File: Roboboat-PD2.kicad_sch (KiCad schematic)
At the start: 29 parts, among them J1 12V, J10 Motor, J11 Motor, J12 Motor, J13 Motor, J14 5V, J15 14.4V, J16 PGOOD, J2 Bucky, J3 Jetson, J4 Motor, J5 Motor, J6 Motor, J7 Motor, J8 Motor, J9 Motor, SW1 Jumper, U1 AOZ2367QI-11

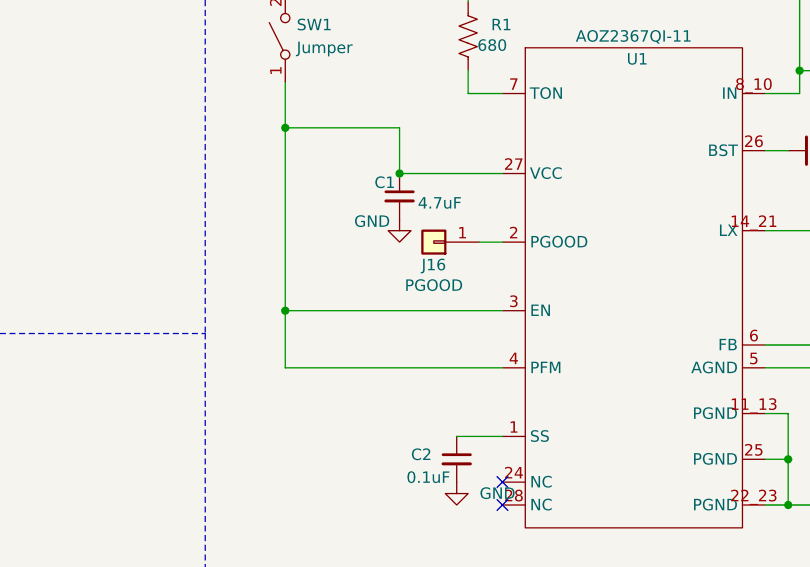
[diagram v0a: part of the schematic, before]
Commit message: add 0.1uF capacitor to PGOOD
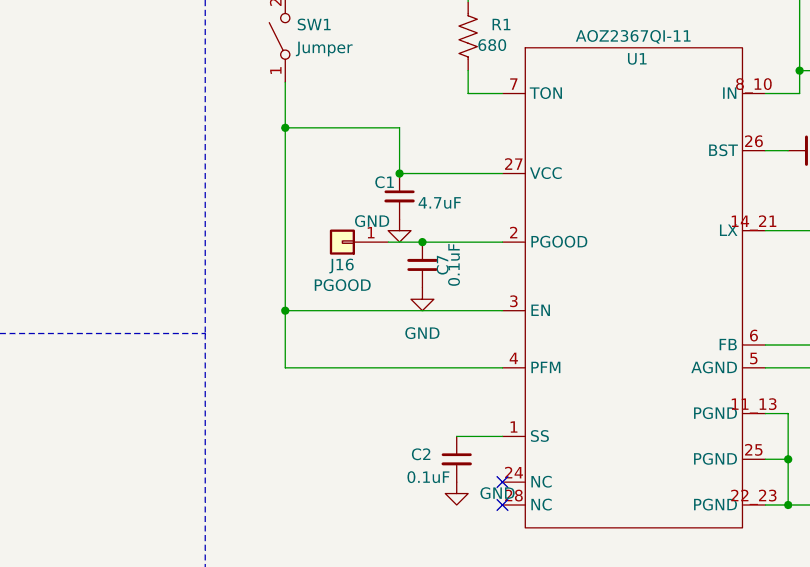
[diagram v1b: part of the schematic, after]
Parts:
- added C7: 0.1uF, Capacitor_SMD:C_1206_3216Metric, symbol Device:C_Small
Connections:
- net GND: now also C7.1
- net at J16.1 (Pin_1), U1.2 (PGOOD): now also C7.2
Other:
- moved on the sheet: J16
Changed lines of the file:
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@@
 	)
 	(junction
+		(at 118.11 66.04)
+		(diameter 0)
+		(color 0 0 0 0)
+	)
+	(junction
 		(at 49.53 110.49)
 		(diameter 0)
@@
 	(wire
 		(pts
-			(xy 124.46 66.04) (xy 127 66.04)
+			(xy 114.3 66.04) (xy 118.11 66.04)
 		)
 		(stroke
@@
 	(wire
 		(pts
+			(xy 118.11 66.04) (xy 127 66.04)
+		)
+		(stroke
+			(width 0)
+			(type default)
+		)
+	)
+	(wire
+		(pts
 			(xy 172.72 64.77) (xy 173.99 64.77)
 		)
@@
 	(symbol
 		(lib_id "power:GND")
+		(at 118.11 71.12 0)
+		(unit 1)
+		(exclude_from_sim no)
+		(in_bom yes)
+		(on_board yes)
+		(dnp no)
+		(fields_autoplaced yes)
+		(property "Reference" "#PWR019"
+			(at 118.11 77.47 0)
+			(effects
+				(font
+					(size 1.27 1.27)
+				)
+				(hide yes)
+			)
+		)
+		(property "Value" "GND"
+			(at 118.11 76.2 0)
+			(effects
+				(font
+					(size 1.27 1.27)
+				)
+			)
+		)
+		(property "Footprint" ""
+			(at 118.11 71.12 0)
+			(effects
+				(font
+					(size 1.27 1.27)
+				)
+				(hide yes)
+			)
+		)
+		(property "Datasheet" ""
+			(at 118.11 71.12 0)
+			(effects
+				(font
+					(size 1.27 1.27)
+				)
+				(hide yes)
+			)
+		)
+		(property "Description" "Power symbol creates a global label with name \"GND\" , ground"
+			(at 118.11 71.12 0)
+			(effects
+				(font
+					(size 1.27 1.27)
+				)
+				(hide yes)
+			)
+		)
+		(pin "1"
+		)
+		(instances
+			(project ""
+				(path "/9a1496f4-7cef-4d33-8239-9c2f43ceb177"
+					(reference "#PWR019")
+					(unit 1)
+				)
+			)
+		)
+	)
+	(symbol
+		(lib_id "power:GND")
 		(at 54.61 55.88 0)
 		(unit 1)
@@
 	(symbol
 		(lib_id "Device:C_Small")
+		(at 118.11 68.58 180)
+		(unit 1)
+		(exclude_from_sim no)
+		(in_bom yes)
+		(on_board yes)
+		(dnp no)
+		(property "Reference" "C7"
+			(at 120.396 68.58 90)
+			(effects
+				(font
+					(size 1.27 1.27)
+				)
+			)
+		)
+		(property "Value" "0.1uF"
+			(at 121.666 68.58 90)
+			(effects
+				(font
+					(size 1.27 1.27)
+				)
+			)
+		)
+		(property "Footprint" "Capacitor_SMD:C_1206_3216Metric"
+			(at 118.11 68.58 0)
+			(effects
+				(font
+					(size 1.27 1.27)
+				)
+				(hide yes)
+			)
+		)
+		(property "Datasheet" "~"
+			(at 118.11 68.58 0)
+			(effects
+				(font
+					(size 1.27 1.27)
+				)
+				(hide yes)
+			)
+		)
+		(property "Description" "Unpolarized capacitor, small symbol"
+			(at 118.11 68.58 0)
+			(effects
+				(font
+					(size 1.27 1.27)
+				)
+				(hide yes)
+			)
+		)
+		(pin "2"
+		)
+		(pin "1"
+		)
+		(instances
+			(project "Roboboat-PD2"
+				(path "/9a1496f4-7cef-4d33-8239-9c2f43ceb177"
+					(reference "C7")
+					(unit 1)
+				)
+			)
+		)
+	)
+	(symbol
+		(lib_id "Device:C_Small")
 		(at 180.34 49.53 0)
 		(unit 1)
@@
 	(symbol
 		(lib_id "Connector_Generic:Conn_01x01")
-		(at 119.38 66.04 180)
+		(at 109.22 66.04 180)
 		(unit 1)
 		(exclude_from_sim no)
@@
 		(dnp no)
 		(property "Reference" "J16"
-			(at 119.38 68.58 0)
+			(at 109.22 68.58 0)
 			(effects
 				(font
@@
 		)
 		(property "Value" "PGOOD"
-			(at 119.38 70.866 0)
+			(at 109.22 70.866 0)
 			(effects
 				(font
@@
 		)
 		(property "Footprint" "Connector_JST:JST_XH_B1B-XH-AM_1x01_P2.50mm_Vertical"
-			(at 119.38 66.04 0)
+			(at 109.22 66.04 0)
 			(effects
 				(font
@@
 		)
 		(property "Datasheet" "~"
-			(at 119.38 66.04 0)
+			(at 109.22 66.04 0)
 			(effects
 				(font
@@
 		)
 		(property "Description" "Generic connector, single row, 01x01, script generated (kicad-library-utils/schlib/autogen/connector/)"
-			(at 119.38 66.04 0)
+			(at 109.22 66.04 0)
 			(effects
 				(font

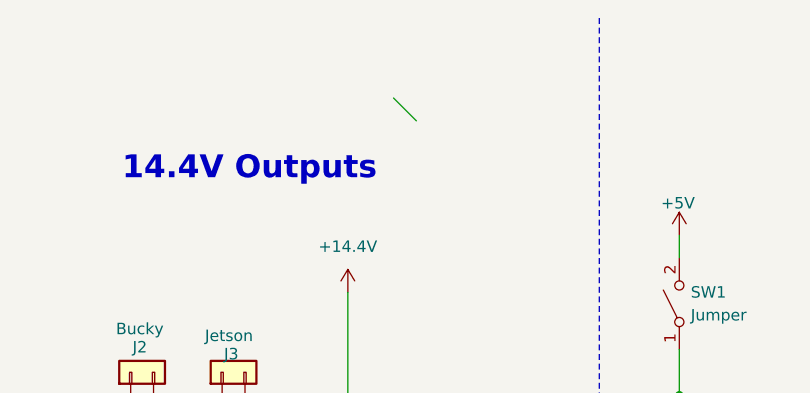
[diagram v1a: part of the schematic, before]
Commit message: move R1, R2, R3, correct fuse footprint
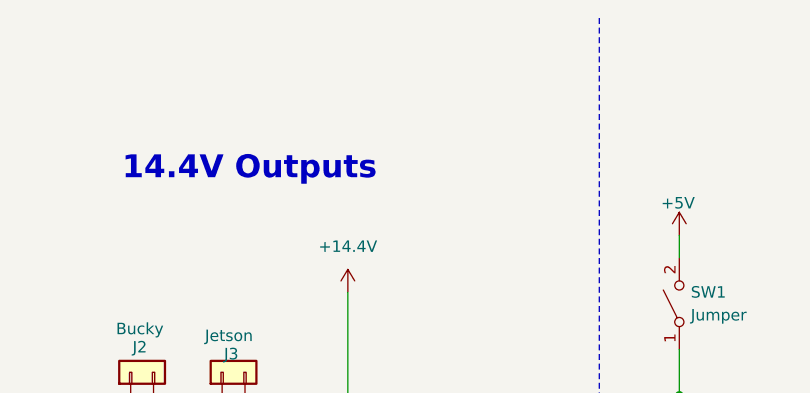
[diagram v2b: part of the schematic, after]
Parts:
- F1: footprint footprints:FUSE_0ZCF0075AF2C -> Fuse:Fuse_1812_4532Metric
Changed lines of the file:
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@@
 		(at 127 92.71)
-	)
-	(bus_entry
-		(at 71.12 20.32)
-		(size 2.54 2.54)
-		(stroke
-			(width 0)
-			(type default)
-		)
 	)
 	(wire
@@
 			)
 		)
-		(property "Footprint" "footprints:FUSE_0ZCF0075AF2C"
+		(property "Footprint" "Fuse:Fuse_1812_4532Metric"
 			(at 52.07 60.96 0)
 			(effects

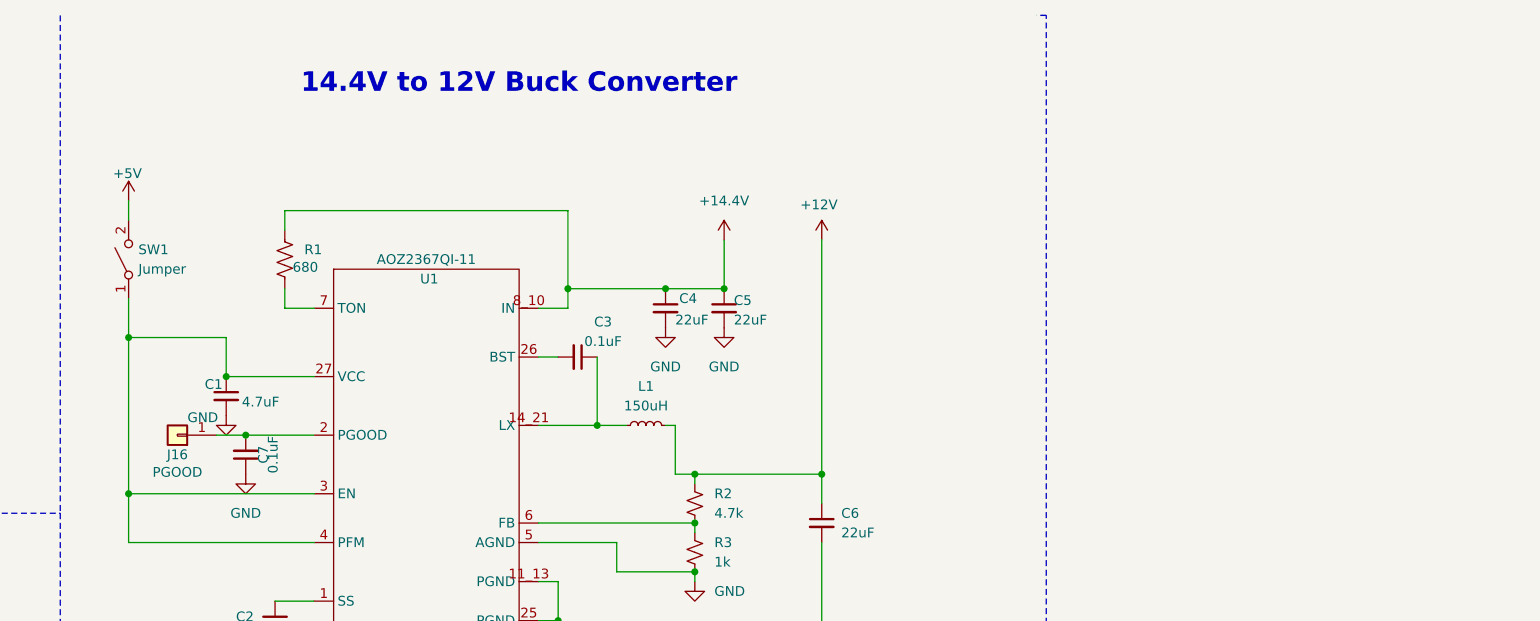
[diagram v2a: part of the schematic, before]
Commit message: add mounting holes and test points to schematic
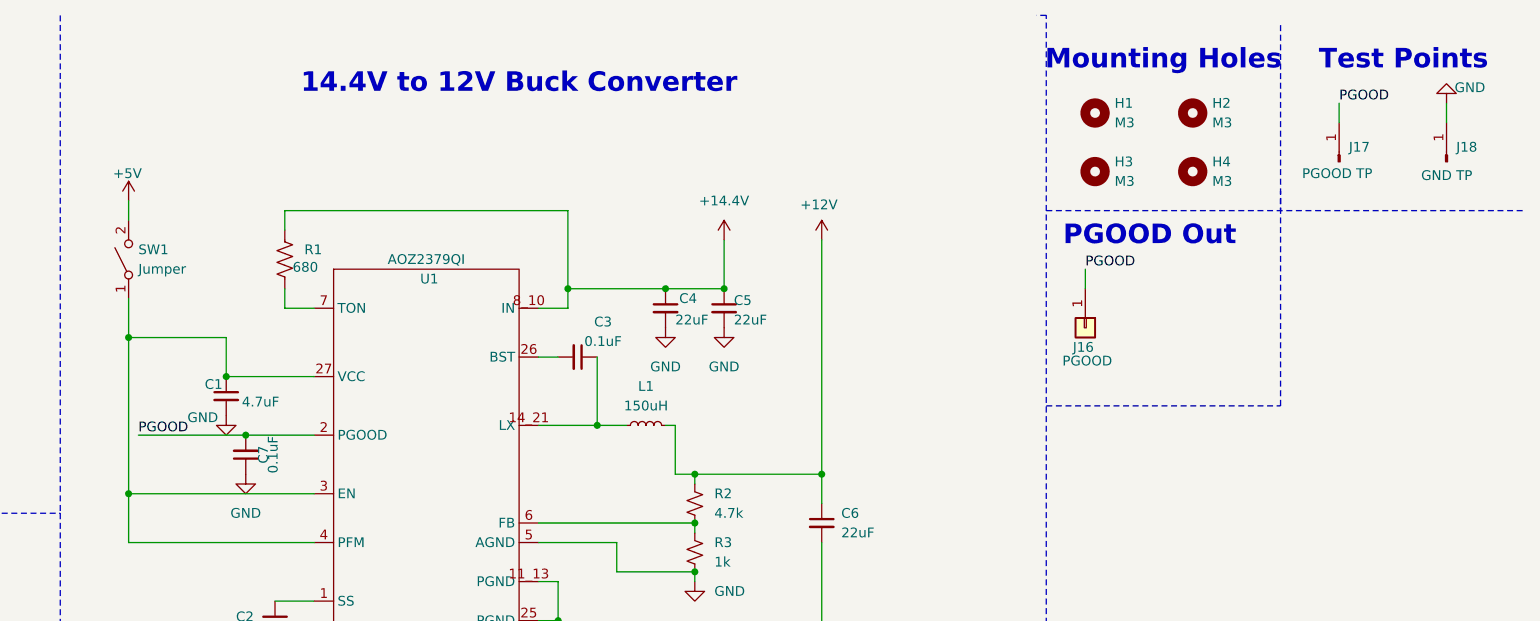
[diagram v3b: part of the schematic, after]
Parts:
- added H1, H2, H3, H4: M3, MountingHole:MountingHole_3.2mm_M3, symbol Mechanical:MountingHole
- added J17: PGOOD TP, TestPoint:TestPoint_Keystone_5010-5014_Multipurpose, symbol Connector:Conn_01x01_Pin
- added J18: GND TP, TestPoint:TestPoint_Keystone_5010-5014_Multipurpose, symbol Connector:Conn_01x01_Pin
- U1: value AOZ2367QI-11 -> AOZ2379QI
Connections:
- net GND: now also J18.1 (Pin_1)
- net PGOOD: now reaches C7.2, J16.1 (Pin_1), U1.2 (PGOOD)
- net PGOOD: now also J17.1 (Pin_1)
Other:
- note added: "Mounting Holes"
- note added: "PGOOD Out"
- note added: "Test Points"

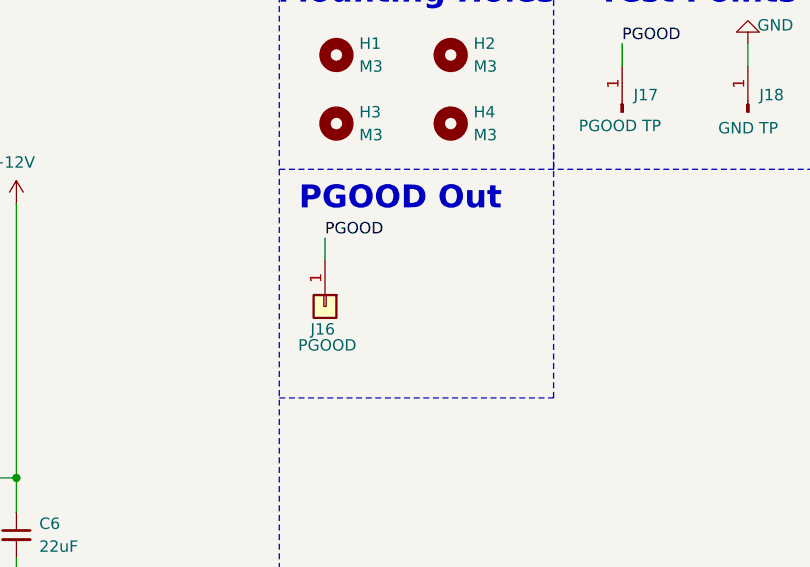
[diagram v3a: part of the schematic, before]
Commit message: add ground to PGOOD output
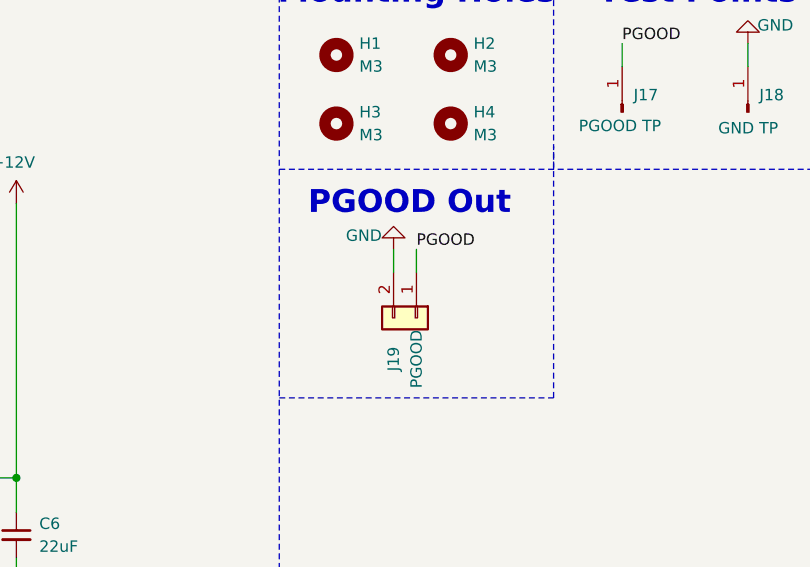
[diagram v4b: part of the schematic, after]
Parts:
- removed J16: PGOOD, Connector_JST:JST_XH_B1B-XH-AM_1x01_P2.50mm_Vertical, symbol Connector_Generic:Conn_01x01
- added J19: PGOOD, Connector_JST:JST_VH_B2P-VH-B_1x02_P3.96mm_Vertical, symbol Connector_Generic:Conn_01x02
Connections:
- net GND: now also J19.2 (Pin_2)
- net PGOOD: now also J19.1 (Pin_1)
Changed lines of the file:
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@@
-	(wire
-		(pts
-			(xy 227.33 44.45) (xy 227.33 46.99)
-		)
-		(stroke
-			(width 0)
-			(type default)
-		)
-	)
 	(wire
 		(pts
@@
 		)
 	)
+	(wire
+		(pts
+			(xy 237.49 45.72) (xy 237.49 48.26)
+		)
+		(stroke
+			(width 0)
+			(type default)
+		)
+	)
 	(polyline
 		(pts
@@
 		(pts
 			(xy 49.53 163.83) (xy 49.53 172.72)
+		)
+		(stroke
+			(width 0)
+			(type default)
+		)
+	)
+	(wire
+		(pts
+			(xy 234.95 45.72) (xy 234.95 48.26)
 		)
 		(stroke
@@
 	(text "PGOOD Out"
 		(exclude_from_sim no)
-		(at 235.712 40.132 0)
+		(at 236.728 40.64 0)
 		(effects
 			(font
@@
 	)
 	(label "PGOOD"
-		(at 227.33 44.45 0)
+		(at 237.49 45.72 0)
 		(fields_autoplaced yes)
 		(effects
@@
 	)
 	(symbol
-		(lib_id "Connector_Generic:Conn_01x01")
-		(at 227.33 52.07 270)
-		(unit 1)
-		(exclude_from_sim no)
-		(in_bom yes)
-		(on_board yes)
-		(dnp no)
-		(property "Reference" "J16"
-			(at 227.076 54.61 90)
-			(effects
-				(font
-					(size 1.27 1.27)
-				)
-			)
-		)
-		(property "Value" "PGOOD"
-			(at 227.584 56.388 90)
-			(effects
-				(font
-					(size 1.27 1.27)
-				)
-			)
-		)
-		(property "Footprint" "Connector_JST:JST_XH_B1B-XH-AM_1x01_P2.50mm_Vertical"
-			(at 227.33 52.07 0)
-			(effects
-				(font
-					(size 1.27 1.27)
-				)
-				(hide yes)
-			)
-		)
-		(property "Datasheet" "~"
-			(at 227.33 52.07 0)
-			(effects
-				(font
-					(size 1.27 1.27)
-				)
-				(hide yes)
-			)
-		)
-		(property "Description" "Generic connector, single row, 01x01, script generated (kicad-library-utils/schlib/autogen/connector/)"
-			(at 227.33 52.07 0)
-			(effects
-				(font
-					(size 1.27 1.27)
-				)
-				(hide yes)
-			)
-		)
-		(pin "1"
-		)
-		(instances
-			(project "Roboboat-PD2"
-				(path "/9a1496f4-7cef-4d33-8239-9c2f43ceb177"
-					(reference "J16")
-					(unit 1)
-				)
-			)
-		)
-	)
-	(symbol
 		(lib_id "power:GND")
 		(at 172.72 52.07 0)
@@
 	)
 	(symbol
+		(lib_id "power:GND")
+		(at 234.95 45.72 180)
+		(unit 1)
+		(exclude_from_sim no)
+		(in_bom yes)
+		(on_board yes)
+		(dnp no)
+		(property "Reference" "#PWR031"
+			(at 234.95 39.37 0)
+			(effects
+				(font
+					(size 1.27 1.27)
+				)
+				(hide yes)
+			)
+		)
+		(property "Value" "GND"
+			(at 231.648 44.196 0)
+			(effects
+				(font
+					(size 1.27 1.27)
+				)
+			)
+		)
+		(property "Footprint" ""
+			(at 234.95 45.72 0)
+			(effects
+				(font
+					(size 1.27 1.27)
+				)
+				(hide yes)
+			)
+		)
+		(property "Datasheet" ""
+			(at 234.95 45.72 0)
+			(effects
+				(font
+					(size 1.27 1.27)
+				)
+				(hide yes)
+			)
+		)
+		(property "Description" "Power symbol creates a global label with name \"GND\" , ground"
+			(at 234.95 45.72 0)
+			(effects
+				(font
+					(size 1.27 1.27)
+				)
+				(hide yes)
+			)
+		)
+		(pin "1"
+		)
+		(instances
+			(project ""
+				(path "/9a1496f4-7cef-4d33-8239-9c2f43ceb177"
+					(reference "#PWR031")
+					(unit 1)
+				)
+			)
+		)
+	)
+	(symbol
 		(lib_id "Connector_Generic:Conn_01x02")
 		(at 34.29 107.95 180)
@@
 					(unit 1)
 				)
+			)
+		)
+	)
+	(symbol
+		(lib_id "Connector_Generic:Conn_01x02")
+		(at 237.49 53.34 270)
+		(unit 1)
+		(exclude_from_sim no)
+		(in_bom yes)
+		(on_board yes)
+		(dnp no)
+		(property "Reference" "J19"
+			(at 234.95 57.912 0)
+			(effects
+				(font
+					(size 1.27 1.27)
+				)
+			)
+		)
+		(property "Value" "PGOOD"
+			(at 237.49 57.912 0)
+			(effects
+				(font
+					(size 1.27 1.27)
+				)
+			)
+		)
+		(property "Footprint" "Connector_JST:JST_VH_B2P-VH-B_1x02_P3.96mm_Vertical"
+			(at 237.49 53.34 0)
+			(effects
+				(font
+					(size 1.27 1.27)
+				)
+				(hide yes)
+			)
+		)
+		(property "Datasheet" "~"
+			(at 237.49 53.34 0)
+			(effects
+				(font
+					(size 1.27 1.27)
+				)
+				(hide yes)
+			)
+		)
+		(property "Description" "Generic connector, single row, 01x02, script generated (kicad-library-utils/schlib/autogen/connector/)"
+			(at 237.49 53.34 0)
+			(effects
+				(font
+					(size 1.27 1.27)
+				)
+				(hide yes)
+			)
+		)
+		(pin "2"
+		)
+		(pin "1"
+		)
+		(instances
+			(project "Roboboat-PD2"
+				(path "/9a1496f4-7cef-4d33-8239-9c2f43ceb177"
+					(reference "J19")
+					(unit 1)
+				)
